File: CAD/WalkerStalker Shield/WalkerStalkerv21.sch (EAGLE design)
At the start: 25 parts

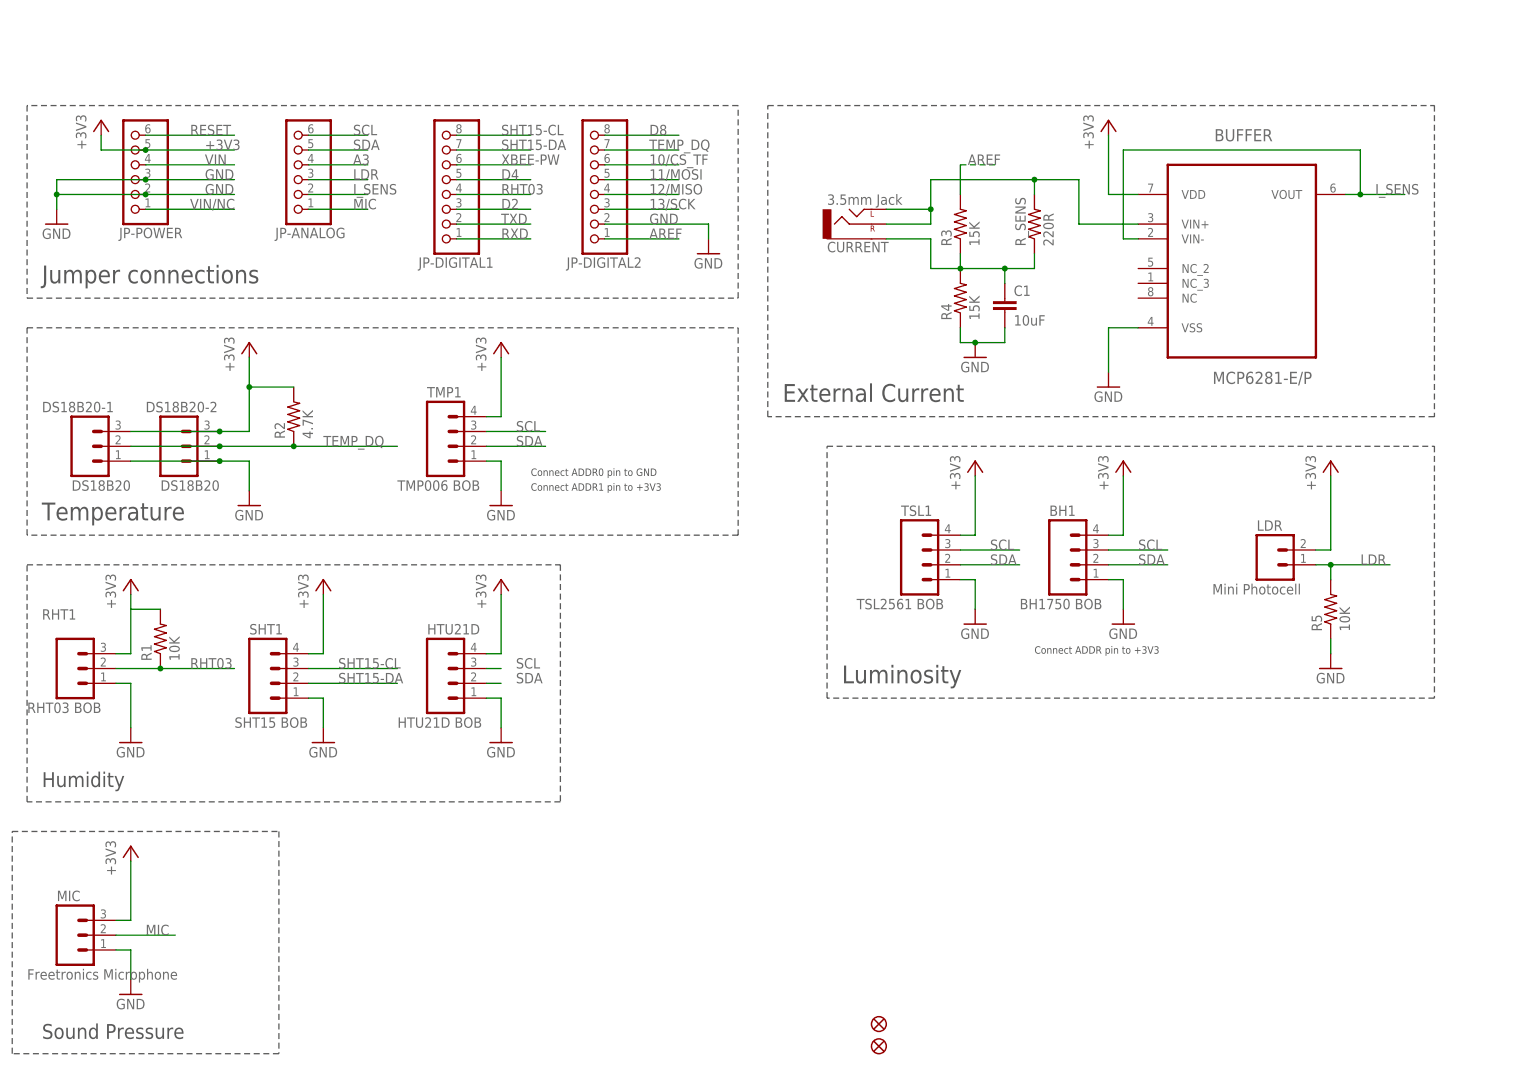
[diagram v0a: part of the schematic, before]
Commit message: Fixed Temperature sensors
+ Temperature sensors are now called by explicit address, rather than
index, which was not consistent (could not tell if sensor was wall or
air)
+ Unit IDs are not transmitted in data packets for easy identification
+Mounting bracket for TMP006 sensor added (3D file)
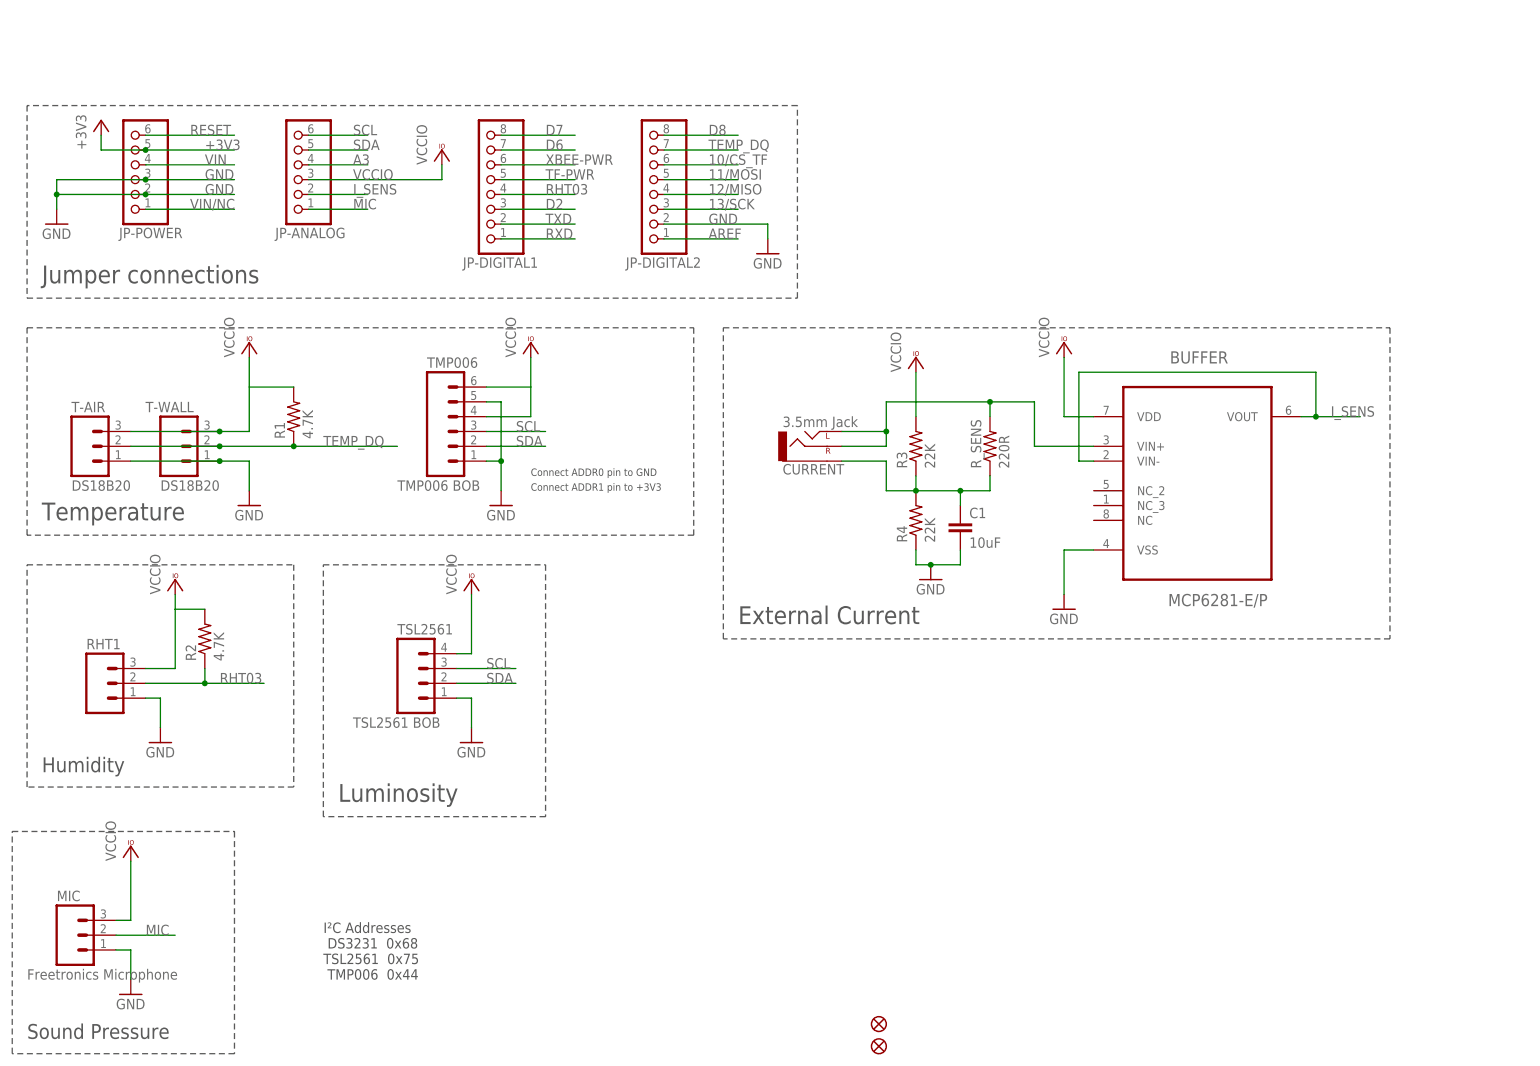
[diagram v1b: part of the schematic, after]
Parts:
- removed BH1: BH1750 BOB, SparkFun-Connectors:M04POLAR
- removed DS18B20-1, DS18B20-2: DS18B20, SparkFun-Connectors:M03POLAR
- removed HTU21D: HTU21D BOB, SparkFun-Connectors:M04POLAR
- removed LDR: Mini Photocell, SparkFun-Connectors:M02POLAR
- removed R5: 10K, SparkFun-Resistors:RESISTOR1206
- removed SHT1: SHT15 BOB, SparkFun-Connectors:M04POLAR
- removed TMP1: TMP006 BOB, SparkFun-Connectors:M04POLAR
- removed TSL1: TSL2561 BOB, SparkFun-Connectors:M04POLAR
- added T-AIR, T-WALL: DS18B20, SparkFun-Connectors:M03PTH
- added TMP006: TMP006 BOB, SparkFun-Connectors:M06SIP
- added TSL2561: TSL2561 BOB, SparkFun-Connectors:M04PTH
- MIC: device SparkFun-Connectors:M03POLAR -> SparkFun-Connectors:M03PTH
- R1: value 10K -> 4.7K
- R3, R4: value 15K -> 22K
- RHT1: value RHT03 BOB -> RHT03; device SparkFun-Connectors:M03POLAR -> SparkFun-Connectors:M03PTH
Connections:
- net D4 renamed TF-PWR
- net XBEE-PW renamed XBEE-PWR
- removed net LDR: JP-ANALOG.3, LDR.1, R5.2
- removed net SHT15-CL: JP-DIGITAL1.8, SHT1.3
- removed net SHT15-DA: JP-DIGITAL1.7, SHT1.2
- new net D6: JP-DIGITAL1.7
- new net D7: JP-DIGITAL1.8
- new net VCCIO: BUFFER.VDD, JP-ANALOG.3, MIC.3, R1.2, R2.2, R3.2, RHT1.3, T-AIR.3, T-WALL.3, TMP006.4, TMP006.6, TSL2561.4
- net +3V3: no longer BH1.4, BUFFER.VDD, DS18B20-1.3, DS18B20-2.3, HTU21D.4, LDR.2, MIC.3, R1.2, R2.2, RHT1.3, SHT1.4, TMP1.4, TSL1.4
- net AREF: no longer R3.2
- net GND: now also T-AIR.1, T-WALL.1, TMP006.1, TMP006.5, TSL2561.1; no longer BH1.1, DS18B20-1.1, DS18B20-2.1, HTU21D.1, R5.1, SHT1.1, TMP1.1, TSL1.1
- net RHT03: now also R2.1; no longer R1.1
- net SCL: now also TMP006.3, TSL2561.3; no longer BH1.3, HTU21D.3, TMP1.3, TSL1.3
- net SDA: now also TMP006.2, TSL2561.2; no longer BH1.2, HTU21D.2, TMP1.2, TSL1.2
- net TEMP_DQ: now also R1.1, T-AIR.2, T-WALL.2; no longer DS18B20-1.2, DS18B20-2.2, R2.1
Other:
- note added: "I²C Addresses DS3231 0x68 TSL2561 0x75 TMP006 0x44"
- note removed: "Connect ADDR pin to +3V3"
- moved on the sheet: BUFFER, C1, CURRENT, JP-DIGITAL1, JP-DIGITAL2, R1, R2, R3, R4, RHT1, R_SENS
